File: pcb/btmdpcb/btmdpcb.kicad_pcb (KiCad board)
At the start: 2 copper layers, 60 x 25 mm, 65 parts, among them J2 ANT, Q1 AO3401A, Q2 BSD235C, Q3 2N7000, Q4 2N7000, Q5 BSD235C, Q6 2N7000, Q7 AO3401A, Q8 BSD235C, Q9 BSD235C, T1 ED8_4, T2 ED8_4, U1 MC34063AD, U2 AP3402, U4 TP4057, U5 ME6211C33M5

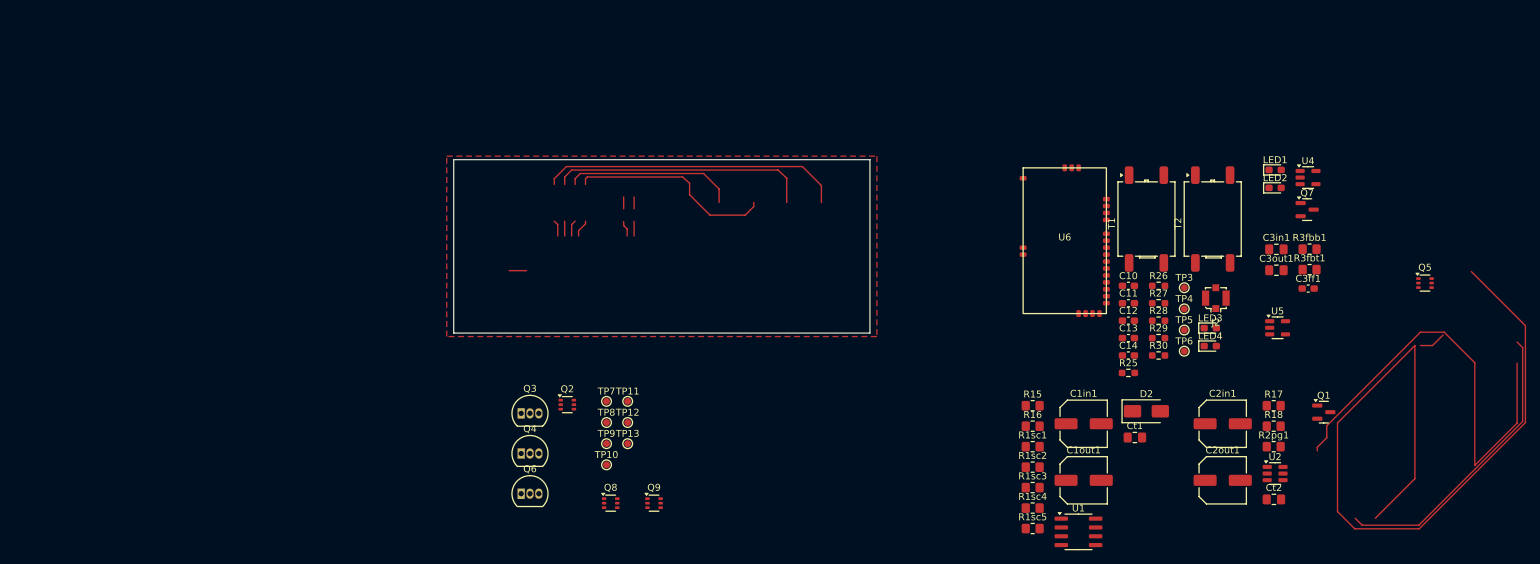
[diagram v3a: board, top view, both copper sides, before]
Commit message: Remove redundant regulators, simplify schematic
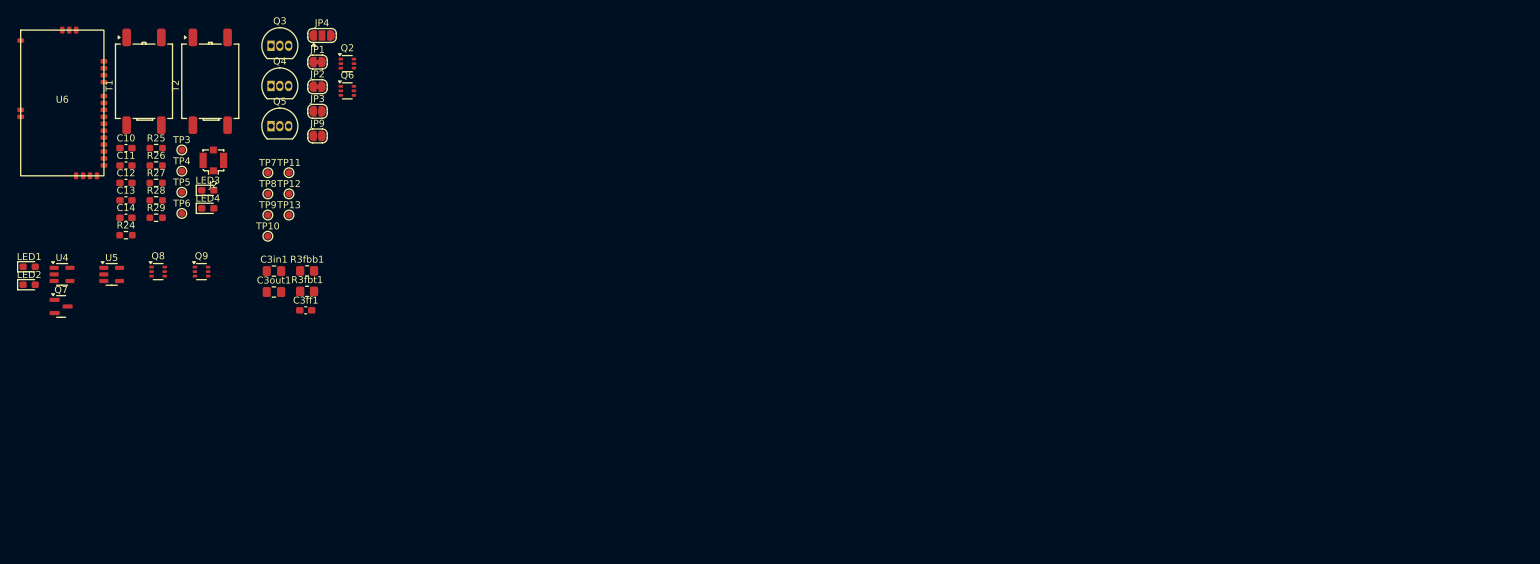
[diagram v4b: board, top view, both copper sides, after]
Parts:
- removed C1in1: 100u, Capacitor_SMD:C_Elec_6.3x7.7
- removed C1out1, C2in1, C2out1: 22u, Capacitor_SMD:C_Elec_6.3x5.4
- removed Ct1: 270p, Capacitor_SMD:C_0805_2012Metric_Pad1.18x1.45mm_HandSolder
- removed Ct2: 245p, Capacitor_SMD:C_0805_2012Metric_Pad1.18x1.45mm_HandSolder
- removed D2: 1N5819, Diode_SMD:D_SMA
- removed Q1: AO3401A, Package_TO_SOT_SMD:SOT-23
- removed R15: 1.5, Resistor_SMD:R_0805_2012Metric_Pad1.20x1.40mm_HandSolder
- removed R16: 7k5, Resistor_SMD:R_0805_2012Metric_Pad1.20x1.40mm_HandSolder
- removed R17: 225k, Resistor_SMD:R_0805_2012Metric_Pad1.20x1.40mm_HandSolder
- removed R18: 150k, Resistor_SMD:R_0805_2012Metric_Pad1.20x1.40mm_HandSolder
- removed R1sc1, R1sc2, R1sc3, R1sc4, R1sc5: 0R2, Resistor_SMD:R_0805_2012Metric_Pad1.20x1.40mm_HandSolder
- removed R2pg1: 100k, Resistor_SMD:R_0805_2012Metric_Pad1.20x1.40mm_HandSolder
- removed R30: 100R, Resistor_SMD:R_0603_1608Metric_Pad0.98x0.95mm_HandSolder
- removed U1: MC34063AD, Package_SO:SOIC-8_3.9x4.9mm_P1.27mm
- removed U2: AP3402, Package_TO_SOT_SMD:TSOT-23-6
- added JP1: SolderJumper_2_Bridged, Jumper:SolderJumper-2_P1.3mm_Bridged_RoundedPad1.0x1.5mm, F.Cu at (98.4, 41.4)
- added JP2: SolderJumper_2_Bridged, Jumper:SolderJumper-2_P1.3mm_Bridged_RoundedPad1.0x1.5mm, F.Cu at (98.4, 45.0)
- added JP3: SolderJumper_2_Open, Jumper:SolderJumper-2_P1.3mm_Open_RoundedPad1.0x1.5mm, F.Cu at (98.4, 48.5)
- added JP4: SolderJumper_3_Open, Jumper:SolderJumper-3_P1.3mm_Open_RoundedPad1.0x1.5mm, F.Cu at (99.0, 37.6)
- added JP9: SolderJumper_2_Open, Jumper:SolderJumper-2_P1.3mm_Open_RoundedPad1.0x1.5mm, F.Cu at (98.4, 52.1)
- added R24: 5k1, Resistor_SMD:R_0603_1608Metric_Pad0.98x0.95mm_HandSolder, F.Cu at (70.8, 66.4)
- Q5: value BSD235C -> 2N7000; footprint Package_TO_SOT_SMD:SOT-363_SC-70-6 -> Package_TO_SOT_THT:TO-92_Inline
- Q6: value 2N7000 -> BSD235C; footprint Package_TO_SOT_THT:TO-92_Inline -> Package_TO_SOT_SMD:SOT-363_SC-70-6
- R28: value 5k1 -> 100R
- moved Q7 180.1 mm to (61.4, 76.7)
- moved LED1 180.1 mm to (56.8, 70.9)
- moved LED2 180.1 mm to (56.8, 73.5)
- moved U4 180.1 mm to (61.6, 72.0)
- moved U5 168.2 mm to (68.7, 72.0)
- moved Q5 167.9 mm to (91.7, 50.7)
- moved C11 145.8 mm to (70.8, 56.3)
- moved C14 145.8 mm to (70.8, 63.9)
- moved J2 145.8 mm to (83.4, 55.6)
- moved LED3 145.8 mm to (82.6, 59.9)
- moved LED4 145.8 mm to (82.6, 62.5)
- moved T1 145.8 mm to (73.4, 44.2)
- moved TP4 145.8 mm to (78.8, 57.2)
- moved C10 145.8 mm to (70.8, 53.8)
- moved C12 145.8 mm to (70.8, 58.9)
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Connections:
- Q5 pad 3: EN_1V5 -> ~{EN_1V5}
- Q6 pad 2: VBUS -> Net-(JP9-A)
- Q6 pad 3: ~{EN_1V5} -> EN_1V5
- R25 pad 2: Net-(C10-Pad1) -> Net-(C11-Pad1)
- R26 pad 2: Net-(C11-Pad1) -> Net-(C12-Pad1)
- R27 pad 2: Net-(C12-Pad1) -> Net-(C13-Pad1)
- R28 pad 1: Net-(R28-Pad1) -> Net-(U6-LED1)
- R28 pad 2: Net-(C13-Pad1) -> Net-(LED3-K)
- R29 pad 1: Net-(U6-LED1) -> Net-(U6-LED2)
- R29 pad 2: Net-(LED3-K) -> Net-(LED4-K)
- T1 pad 3: Net-(R26-Pad1) -> Net-(R25-Pad1)
- T1 pad 4: Net-(R25-Pad1) -> Net-(R24-Pad1)
- T2 pad 3: Net-(R27-Pad1) -> Net-(R26-Pad1)
- T2 pad 4: Net-(R28-Pad1) -> Net-(R27-Pad1)
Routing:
- net (no net): track 375.9 -> 0.00 mm
- net Net-(J2-In): track 2.50 -> 0.00 mm
- net Net-(LED2-K): track 1.71 -> 0.00 mm
- net Net-(LED1-K): track 1.71 -> 0.00 mm
- removed copper zone on F.Cu, net GND
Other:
- board outline removed

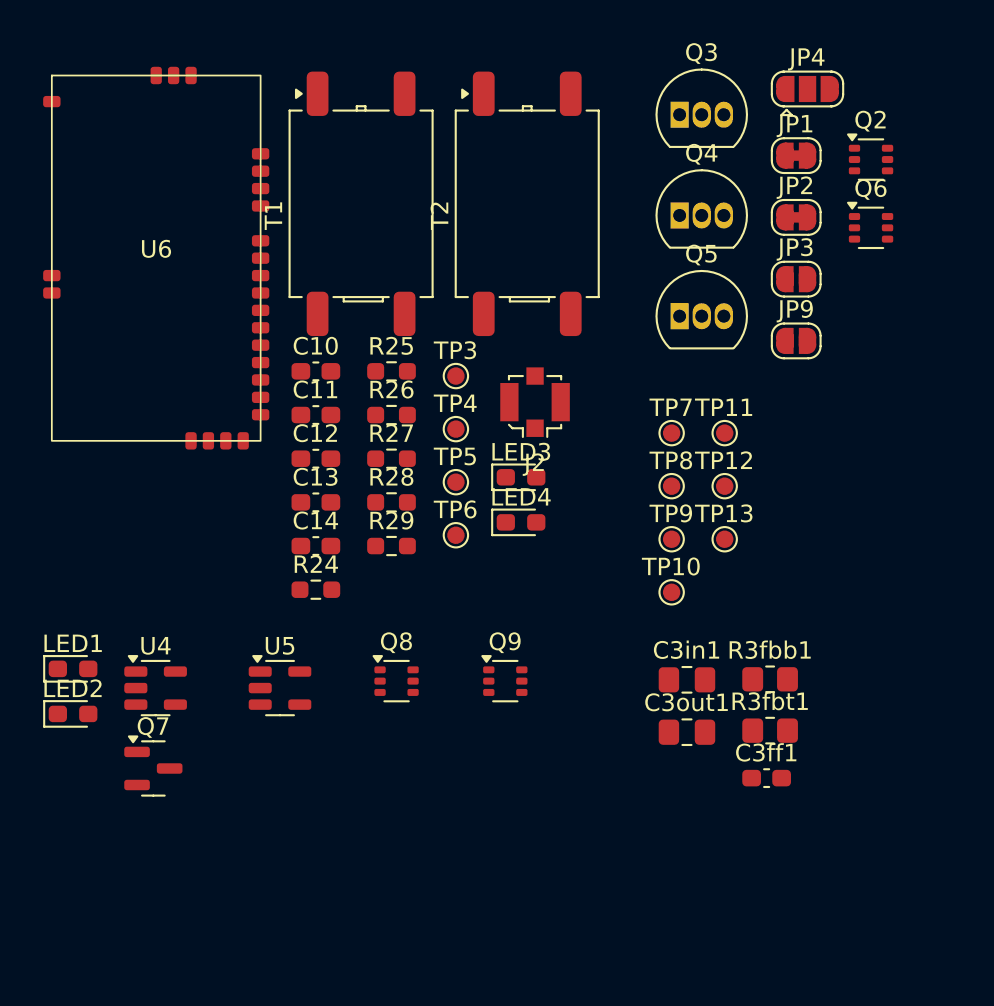
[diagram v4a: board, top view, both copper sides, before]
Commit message: Create and use BSD235N symbol
to replace 2N7000 N-MOSFETS used temporarily up to now
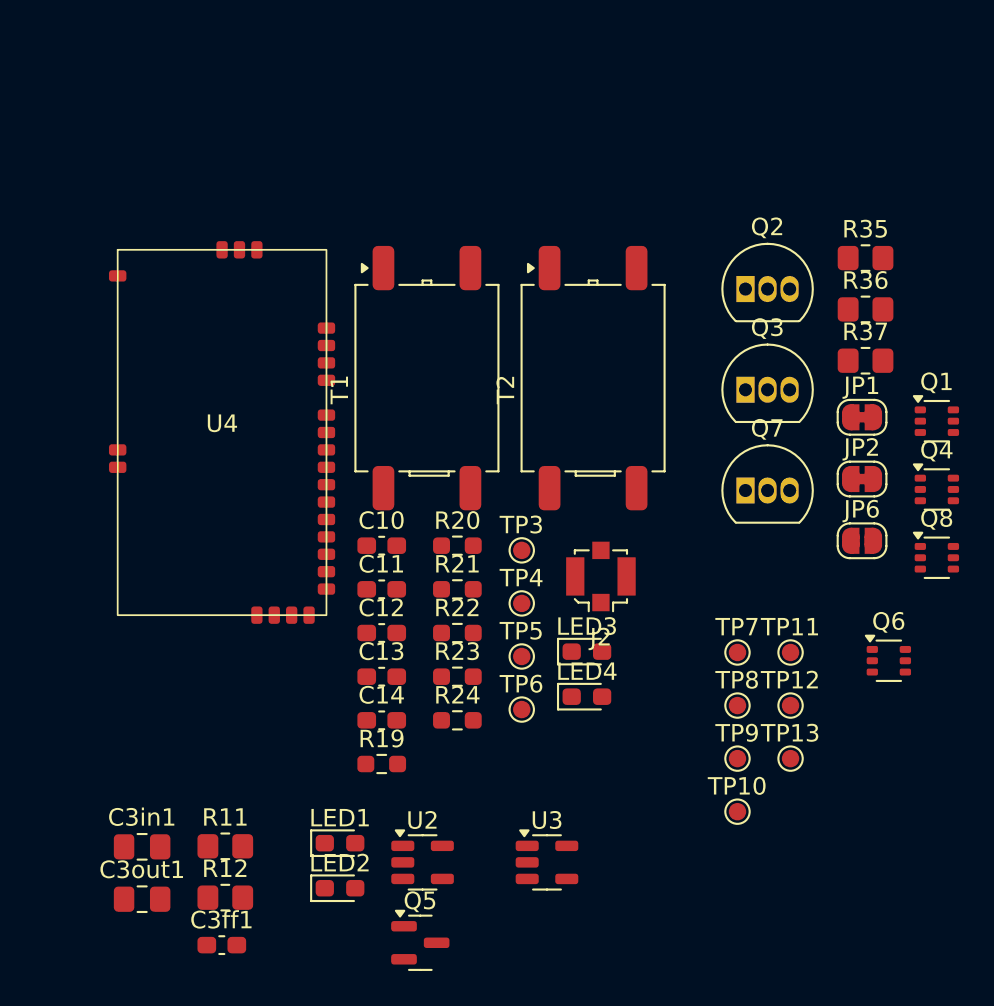
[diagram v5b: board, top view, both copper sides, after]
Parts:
- removed JP3, JP9: SolderJumper_2_Open, Jumper:SolderJumper-2_P1.3mm_Open_RoundedPad1.0x1.5mm
- removed JP4: SolderJumper_3_Open, Jumper:SolderJumper-3_P1.3mm_Open_RoundedPad1.0x1.5mm
- removed Q9: BSD235C, Package_TO_SOT_SMD:SOT-363_SC-70-6
- removed R25, R26, R27: 5k1, Resistor_SMD:R_0603_1608Metric_Pad0.98x0.95mm_HandSolder
- removed R28, R29: 100R, Resistor_SMD:R_0603_1608Metric_Pad0.98x0.95mm_HandSolder
- removed R3fbb1: 115k, Resistor_SMD:R_0805_2012Metric_Pad1.20x1.40mm_HandSolder
- removed R3fbt1: 100k, Resistor_SMD:R_0805_2012Metric_Pad1.20x1.40mm_HandSolder
- removed U5: ME6211C33M5, Package_TO_SOT_SMD:SOT-23-5
- removed U6: ~, bt_audio:bt_audio_smd
- added JP6: SolderJumper_2_Open, Jumper:SolderJumper-2_P1.3mm_Open_RoundedPad1.0x1.5mm, F.Cu at (102.2, 63.6)
- added Q1: BSD235C, Package_TO_SOT_SMD:SOT-363_SC-70-6, F.Cu at (106.5, 56.7)
- added R11: 100k, Resistor_SMD:R_0805_2012Metric_Pad1.20x1.40mm_HandSolder, F.Cu at (65.6, 81.1)
- added R12: 115k, Resistor_SMD:R_0805_2012Metric_Pad1.20x1.40mm_HandSolder, F.Cu at (65.6, 84.1)
- added R19: 5k1, Resistor_SMD:R_0603_1608Metric_Pad0.98x0.95mm_HandSolder, F.Cu at (74.5, 76.4)
- added R20: 5k1, Resistor_SMD:R_0603_1608Metric_Pad0.98x0.95mm_HandSolder, F.Cu at (78.9, 63.9)
- added R21: 5k1, Resistor_SMD:R_0603_1608Metric_Pad0.98x0.95mm_HandSolder, F.Cu at (78.9, 66.4)
- added R22: 5k1, Resistor_SMD:R_0603_1608Metric_Pad0.98x0.95mm_HandSolder, F.Cu at (78.9, 68.9)
- added R23: 100R, Resistor_SMD:R_0603_1608Metric_Pad0.98x0.95mm_HandSolder, F.Cu at (78.9, 71.4)
- added R35: R, Resistor_SMD:R_0805_2012Metric_Pad1.20x1.40mm_HandSolder, F.Cu at (102.4, 47.3)
- added R36: R, Resistor_SMD:R_0805_2012Metric_Pad1.20x1.40mm_HandSolder, F.Cu at (102.4, 50.3)
- added R37: R, Resistor_SMD:R_0805_2012Metric_Pad1.20x1.40mm_HandSolder, F.Cu at (102.4, 53.2)
- added U2: TP4057, Package_TO_SOT_SMD:TSOT-23-5, F.Cu at (76.9, 82.1)
- added U3: ME6211C33M5, Package_TO_SOT_SMD:SOT-23-5, F.Cu at (84.0, 82.1)
- Q2: value BSD235C -> 2N7000; footprint Package_TO_SOT_SMD:SOT-363_SC-70-6 -> Package_TO_SOT_THT:TO-92_Inline
- Q4: value 2N7000 -> BSD235C; footprint Package_TO_SOT_THT:TO-92_Inline -> Package_TO_SOT_SMD:SOT-363_SC-70-6
- Q5: value 2N7000 -> AO3401A; footprint Package_TO_SOT_THT:TO-92_Inline -> Package_TO_SOT_SMD:SOT-23
- Q7: value AO3401A -> 2N7000; footprint Package_TO_SOT_SMD:SOT-23 -> Package_TO_SOT_THT:TO-92_Inline
- Q8: value BSD235C -> BSD235N
- R24: value 5k1 -> 100R
- U4: value TP4057 -> ~; footprint Package_TO_SOT_SMD:TSOT-23-5 -> bt_audio:bt_audio_smd
- moved Q5 39.0 mm to (76.8, 86.7)
- moved Q7 37.6 mm to (95.5, 60.7)
- moved C3in1 32.8 mm to (60.8, 81.2)
- moved C3out1 32.8 mm to (60.8, 84.2)
- moved C3ff1 32.8 mm to (65.4, 86.8)
- moved Q8 31.9 mm to (106.5, 64.5)
- moved Q6 24.9 mm to (103.7, 70.5)
- moved Q4 21.6 mm to (106.5, 60.6)
- moved LED2 18.3 mm to (72.2, 83.5)
- moved LED1 18.3 mm to (72.2, 81.0)
- moved Q3 16.3 mm to (95.5, 54.9)
- moved JP1 15.5 mm to (102.2, 56.5)
- moved JP2 15.5 mm to (102.2, 60.0)
- moved U4 15.2 mm to (65.4, 57.4)
- moved TP11 13.2 mm to (98.0, 70.0)
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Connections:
- C10 pad 2: Net-(U6-L+) -> Net-(U4-L+)
- C11 pad 2: Net-(U6-L-) -> Net-(U4-L-)
- C12 pad 2: Net-(U6-R-) -> Net-(U4-R-)
- C13 pad 2: Net-(U6-R+) -> Net-(U4-R+)
- Q2 pad 2: /HOLD -> /KICKSTART/BT_BTN
- Q2 pad 3: Net-(Q2B-DP) -> ~{EN_1V5}
- Q3 pad 2: /HOLD -> VDD
- Q3 pad 3: Net-(Q3-D) -> ~{EN_1V5}
- Q4 pad 2: Net-(Q3-D) -> Net-(JP6-A)
- Q4 pad 3: ~{EN_1V5} -> EN_1V5
- Q5 pad 1: GND -> VBUS
- Q5 pad 2: VDD -> +BATT
- Q5 pad 3: ~{EN_1V5} -> Net-(BT1-+)
- Q6 pad 2: Net-(JP9-A) -> /HOLD
- Q6 pad 3: EN_1V5 -> /HOLD
- Q6 pad 5: ~{EN_1V5} -> /~{HOLD}
- Q6 pad 6: ~{EN_1V5} -> /MD unit (MZ-N505)/~{SW_HOLD}_IN
- Q7 pad 1: VBUS -> GND
- Q7 pad 2: +BATT -> Net-(Q7-G)
- Q7 pad 3: Net-(BT1-+) -> Net-(Q7-D)
- Q8 pad 1: GND -> Net-(Q8A-S1)
- Q8 pad 2: /HOLD -> Net-(Q8A-G1)
- Q8 pad 3: /HOLD -> Net-(Q8B-D2)
- Q8 pad 4: +BATT -> Net-(Q8B-S2)
- Q8 pad 5: /~{HOLD} -> Net-(Q8B-G2)
- Q8 pad 6: /MD unit (MZ-N505)/~{SW_HOLD}_IN -> Net-(Q8A-D1)
- R24 pad 1: Net-(R24-Pad1) -> Net-(U4-LED2)
- R24 pad 2: Net-(C10-Pad1) -> Net-(LED4-K)
- T1 pad 4: Net-(R24-Pad1) -> Net-(R19-Pad1)
- TP11 pad 1: /~{PAUSE} -> /MD unit (MZ-N505)/~{BTN_PAUSE}_IN
- TP12 pad 1: /MD unit (MZ-N505)/~{BTN_REC}_OUT -> /~{REC}
- TP3 pad 1: Net-(U6-BAT+) -> Net-(U4-BAT+)
- U4 pad 1: Net-(LED2-K) -> GND
